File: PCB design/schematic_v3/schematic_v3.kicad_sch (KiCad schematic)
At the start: 111 parts, among them J1 Conn_01x05_Pin, J2 Conn_01x06_Pin, J3 Conn_01x03_Pin, J5 connection_moteur, Q1 IRLB8721PBF, SW1 SW_MEC_5E, U1 LAN9252, U2 STM32F446RETx, U3 HX1188NL, U4 XL1509-3.3, U5 24FC512-I/ST, U6 LMR14030SQDPRTQ1, U7 SP3485CN, Y1 25MHz, Y2 8MHz

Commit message: 03/06
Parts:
- removed C103, C104, C87, C88, C89, C90: 1u, symbol Device:C_Small
- removed C36: 47u, symbol Device:C_Polarized_Small_US
- removed C71: 10u, symbol Device:C_Small
- removed C72, C73: 2.2u, symbol Device:C_Small
- removed C85: 470u, symbol Device:C_Small
- removed C86: 330u, symbol Device:C_Small
- removed C91: 0.1, symbol Device:C_Small
- removed D2: B340, Diode_SMD:D_SMC, symbol Diode:B340
- removed F1: Bourns MF-MSMF250-2, symbol Device:Polyfuse_Small
- removed J1: Conn_01x05_Pin, symbol Connector:Conn_01x05_Pin
- removed J2: Conn_01x06_Pin, symbol Connector:Conn_01x06_Pin
- removed Q1: IRLB8721PBF, footprints:IRLB8721PBF, symbol IRLB8721PBF:IRLB8721PBF
- removed R45: 12.1k, symbol Device:R_Small
- removed SW1: SW_MEC_5E, Button_Switch_SMD:SW_MEC_5GSH9, symbol Switch:SW_MEC_5E
- removed U1: LAN9252, Package_DFN_QFN:QFN-64-1EP_9x9mm_P0.5mm_EP6x6mm, symbol LAN9252:LAN9252_test
- removed U4: XL1509-3.3, Package_SO:SOIC-8_3.9x4.9mm_P1.27mm, symbol Regulator_Switching:XL1509-3.3
- added C1, C11: 0.1u, Capacitor_SMD:C_0603_1608Metric, symbol Device:C_Small
- added C19, C20: 1u, Capacitor_SMD:C_0603_1608Metric, symbol Device:C_Small
- added C56: 10u, Capacitor_SMD:C_1206_3216Metric, symbol Device:C_Small
- added C57: 100n, Capacitor_SMD:C_0603_1608Metric, symbol Device:C_Small
- added C58, C59: 22u, Capacitor_SMD:C_1206_3216Metric, symbol Device:C_Small
- added IC1: LAN9252, footprints:LAN9252, symbol LAN9252:LAN9252
- added J1: Conn_01x04_Pin, Connector_JST:JST_EH_B4B-EH-A_1x04_P2.50mm_Vertical, symbol Connector:Conn_01x04_Pin
- added J3: Conn_01x05_Pin, Connector_PinHeader_1.27mm:PinHeader_1x05_P1.27mm_Vertical, symbol Connector:Conn_01x05_Pin
- added J5: Conn_01x02_Pin, Connector_JST:JST_EH_B2B-EH-A_1x02_P2.50mm_Vertical, symbol Connector:Conn_01x02_Pin
- added Q1: AO3400A, Package_TO_SOT_SMD:SOT-23, symbol Transistor_FET:AO3400A
- added R15, R17, R18: 10k, Resistor_SMD:R_0603_1608Metric, symbol Device:R_Small
- added R16: 12.1k, Resistor_SMD:R_0603_1608Metric, symbol Device:R_Small
- added S1: TS40-66-43-BK-260-SMT-TR, footprints:TS40-66-43-BK-260-SMT-TR, symbol TS40-66-43-BK-260-SMT-TR:TS40-66-43-BK-260-SMT-TR
- added U7: AP63203WU, Package_TO_SOT_SMD:TSOT-23-6, symbol Regulator_Switching:AP63203WU
- C10: renamed from C37; footprint (none) -> Capacitor_SMD:CP_Elec_5x5.4
- C12: renamed from C94; footprint (none) -> Capacitor_SMD:C_0603_1608Metric
- C13: renamed from C102; footprint (none) -> Capacitor_SMD:C_0603_1608Metric
- C14: renamed from C95; footprint (none) -> Capacitor_SMD:C_0603_1608Metric
- C15: renamed from C101; footprint (none) -> Capacitor_SMD:C_0603_1608Metric
- C16: renamed from C96; footprint (none) -> Capacitor_SMD:C_0603_1608Metric
- C17: renamed from C100; footprint (none) -> Capacitor_SMD:C_0603_1608Metric
- C18: renamed from C35; footprint (none) -> Capacitor_SMD:CP_Elec_5x5.4
- C2: renamed from C66; footprint (none) -> Capacitor_SMD:C_0603_1608Metric
- C21: renamed from C97; footprint (none) -> Capacitor_SMD:C_0603_1608Metric
- C22: renamed from C99; footprint (none) -> Capacitor_SMD:C_0603_1608Metric
- C26: renamed from C92; footprint (none) -> Capacitor_SMD:C_0603_1608Metric
- C27: renamed from C93; footprint (none) -> Capacitor_SMD:C_0603_1608Metric
- C28: renamed from C98; footprint (none) -> Capacitor_SMD:C_0603_1608Metric
- C29: renamed from C70; footprint (none) -> Capacitor_SMD:C_1206_3216Metric
- C3: renamed from C67; footprint (none) -> Capacitor_SMD:C_0603_1608Metric
- C30: renamed from C84; footprint (none) -> Capacitor_SMD:C_0603_1608Metric
- C33: renamed from C105; footprint (none) -> Capacitor_SMD:C_0603_1608Metric
- C35: renamed from C106; footprint (none) -> Capacitor_SMD:C_0603_1608Metric
- C38: renamed from C74; footprint (none) -> Capacitor_SMD:C_1206_3216Metric
- C39: renamed from C108; footprint (none) -> Capacitor_SMD:C_0603_1608Metric
- C4: renamed from C80; footprint (none) -> Capacitor_SMD:C_0603_1608Metric
- C40: renamed from C110; footprint (none) -> Capacitor_SMD:C_0603_1608Metric
- C41: renamed from C109; footprint (none) -> Capacitor_SMD:C_0603_1608Metric
- C42: renamed from C75; footprint (none) -> Capacitor_SMD:C_0603_1608Metric
- C43: renamed from C111; footprint (none) -> Capacitor_SMD:C_0603_1608Metric
- C44: renamed from C112; footprint (none) -> Capacitor_SMD:C_0603_1608Metric
- C45: renamed from C107; footprint (none) -> Capacitor_SMD:C_0603_1608Metric
- C46: renamed from C113; footprint (none) -> Capacitor_SMD:C_0603_1608Metric
- C47: renamed from C114; footprint (none) -> Capacitor_SMD:C_0603_1608Metric
- C48: renamed from C115; footprint (none) -> Capacitor_SMD:C_0603_1608Metric
- C5: renamed from C81; footprint (none) -> Capacitor_SMD:C_0603_1608Metric
- C50: renamed from C76; footprint (none) -> Capacitor_SMD:C_0603_1608Metric
- C51: renamed from C116; footprint (none) -> Capacitor_SMD:C_0603_1608Metric
- C52: renamed from C77; footprint (none) -> Capacitor_SMD:C_0603_1608Metric
- C53: renamed from C78; footprint (none) -> Capacitor_SMD:C_1206_3216Metric
- C55: renamed from C79; footprint (none) -> Capacitor_SMD:C_1206_3216Metric
- C6: renamed from C117; footprint (none) -> Capacitor_SMD:C_0603_1608Metric
- C7: renamed from C82; footprint (none) -> Capacitor_SMD:C_0603_1608Metric
- C8: renamed from C40; footprint (none) -> Capacitor_SMD:CP_Elec_5x5.4
- C9: renamed from C83; footprint (none) -> Capacitor_SMD:C_0603_1608Metric
- FB1, FB2, FB3, FB4: footprint footprints:LMR14030SQDPRTQ1 -> footprints:IND_BLM18_0603_MUR
- L1: footprint (none) -> Inductor_SMD:L_Bourns_SRR1260
- L3: value 47u -> 6.8u; footprint Inductor_SMD_Wurth:L_Wurth_WE-LQSH-4020 -> Inductor_SMD:L_Bourns-SRN4018; Field5 (none) -> 4040; Field6 (none) -> 3A
- R1: renamed from R30; footprint (none) -> Resistor_SMD:R_0603_1608Metric
- R10: renamed from R53; footprint (none) -> Resistor_SMD:R_0805_2012Metric
- R11: renamed from R35; footprint (none) -> Resistor_SMD:R_0603_1608Metric
- R12: renamed from R36; footprint (none) -> Resistor_SMD:R_0603_1608Metric
- R13: renamed from R58; footprint (none) -> Resistor_SMD:R_0603_1608Metric
- R14: renamed from R59; footprint (none) -> Resistor_SMD:R_0603_1608Metric
- R19: renamed from R42; footprint (none) -> Resistor_SMD:R_0603_1608Metric
- R2: renamed from R56; footprint (none) -> Resistor_SMD:R_0603_1608Metric
- R20: renamed from R46; footprint (none) -> Resistor_SMD:R_0603_1608Metric
- R21: renamed from R43; footprint (none) -> Resistor_SMD:R_0603_1608Metric
- R22: renamed from R44; footprint (none) -> Resistor_SMD:R_0603_1608Metric
- R23: renamed from R37; footprint (none) -> Resistor_SMD:R_0603_1608Metric
- R24: renamed from R38; footprint (none) -> Resistor_SMD:R_0603_1608Metric
- R25: renamed from R39; footprint (none) -> Resistor_SMD:R_0603_1608Metric
- R26: renamed from R47; footprint (none) -> Resistor_SMD:R_0603_1608Metric
- R27: renamed from R52; footprint (none) -> Resistor_SMD:R_0603_1608Metric
- R28: renamed from R40; footprint (none) -> Resistor_SMD:R_0603_1608Metric
- R29: renamed from R41; footprint (none) -> Resistor_SMD:R_0603_1608Metric
- R3: renamed from R57; footprint (none) -> Resistor_SMD:R_0603_1608Metric
- R30: renamed from R48; footprint (none) -> Resistor_SMD:R_0603_1608Metric
- R31: renamed from R51; footprint (none) -> Resistor_SMD:R_0603_1608Metric
- R32: renamed from R49; footprint (none) -> Resistor_SMD:R_0603_1608Metric
- R33: renamed from R50; footprint (none) -> Resistor_SMD:R_0603_1608Metric
- R4: renamed from R31; footprint (none) -> Resistor_SMD:R_0603_1608Metric
- R5: renamed from R32; footprint (none) -> Resistor_SMD:R_0603_1608Metric
- R6: renamed from R33; footprint (none) -> Resistor_SMD:R_0603_1608Metric
- R7: renamed from R34; footprint (none) -> Resistor_SMD:R_0603_1608Metric
- R8: renamed from R54; footprint (none) -> Resistor_SMD:R_0603_1608Metric
- R9: renamed from R55; footprint (none) -> Resistor_SMD:R_0603_1608Metric
- renumbered D4 to D1, D5 to D2, FB6 to FB5, J5 to J2, J3 to J4, U3 to U1, U7 to U2, U5 to U3, U6 to U4, U2 to U5
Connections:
- net VDD12TX is gone; now on net +3.3V: FB4.2
- net VDD12TX2 is gone; now on net VDD12TX1: C33.1
- net +12V: now also D1.2 (A), C56.1, U7.2 (EN), U7.3 (IN); no longer D1.1 (K)
- net +3.3V: now also FB1.1, C58.1, C59.1, IC1.14 (VDDIO0), IC1.20 (VDDIO1), IC1.32 (VDDIO2), IC1.37 (VDDIO3), IC1.47 (VDDIO4), IC1.5 (VDD33), IC1.7 (REG_EN), J3.4 (Pin_4), R15.1, U7.1 (FB); no longer FB1.2, FB2.2
- net GND: now also C1.1, C11.1, C19.2, C20.2, C56.2, C58.2, C59.2, IC1.10 (FXSDB/FXLOSB/FXSDENB), IC1.4 (OSCVSS), IC1.40 (D8/AD8/DIGIO2/GPI2/GPO2/MII_MDIO), IC1.41 (TESTMODE), IC1.65 (VSS), IC1.8 (FXLOSEN), IC1.9 (FXSDA/FXLOSA/FXSDENA), J3.3 (Pin_3), J5.1 (Pin_1), Q1.2 (S), R16.1, R17.1, R18.1, S1.1 (COM_1), S1.2 (COM_2), U7.4 (GND)
- net I2C_SCL: now also IC1.43 (EESCL/TCK)
- net I2C_SDL: now also IC1.42 (EESDA/TMS)
- net IRQ: now also IC1.44 (IRQ)
- net MISO: now also IC1.13 (D1/AD1/EOF/SO/SIO1)
- net MOSI: now also IC1.17 (D0/AD0/WD_STATE/SI/SIO0)
- net NRST: now also J3.5 (Pin_5), S1.3 (NO_1), S1.4 (NO_2)
- net OSCI: now also IC1.1 (OSCI)
- net OSCO: now also IC1.2 (OSCO)
- net RST#: now also IC1.11 (RST#)
- net RXA_N: now also IC1.54 (RXNA)
- net RXA_P: now also IC1.55 (RXPA)
- net SCK: now also IC1.19 (D9/AD9/LATCH_IN/SCK)
- net SCS#: now also IC1.50 (D5/AD5/OUTVALID/SCS#)
- net SWCLK: now also J3.2 (Pin_2)
- net SWDIO: now also J3.1 (Pin_1)
- net SYNC0: now also IC1.34 (SYNC0/LATCH0)
- net TXA_N: now also IC1.52 (TXNA)
- net TXA_P: now also IC1.53 (TXPA)
- net VDD12TX1: now also FB2.2, IC1.56 (VDD12TX1), IC1.59 (VDD12TX2)
- net VDD33TXRX1: now also FB3.1, C19.1, IC1.51 (VDD33TXRX1); no longer FB1.1
- net VDD33TXRX2: now also FB4.1, C20.1, IC1.64 (VDD33TXRX2); no longer FB2.1
- net VDDCR: now also FB2.1, C1.2, IC1.24 (VDDCR1), IC1.3 (OSCVDD12), IC1.38 (VDDCR2), IC1.6 (VDDCR0); no longer FB4.1
- net +36V: now reaches D2.2 (A)
- net +36V: now also J5.2 (Pin_2)
- net at U1.11 (RX+): now also J1.2 (Pin_2)
- net at U1.14 (TX-): now also J1.3 (Pin_3)
- net at U1.16 (TX+): now also J1.4 (Pin_4)
- net at U1.9 (RX-): now also J1.1 (Pin_1)
- net at L3.1: now also C57.1, U7.5 (SW)
- net at J2.1 (Pin_1): now also D1.1 (K), Q1.3 (D); no longer D1.2 (A)
- net at R13.1, R14.2: now also Q1.1 (G)
- net at U5.14 (PA0): now also J4.2 (Pin_2); no longer J4.3 (Pin_3)
- net at U5.15 (PA1): now also J4.3 (Pin_3); no longer J4.2 (Pin_2)
- net SMPS_PGOOD: no longer names the net of R23.2, R24.1, U4.8 (PGOOD)
- new net: IC1.48 (LINKACTLED0/TDO/CHIP_MODE0), R18.2
- new net: IC1.57 (RBIAS), R16.2
- new net: IC1.46 (LINKACTLED1/TDI/CHIP_MODE1), R17.2
- new net: C11.2, FB1.2, IC1.58 (VDD33BIAS)
- new net: C57.2, U7.6 (BST)
- new net: IC1.45 (RUNLED/E2PSIZE), R15.2
- no-connect marks 59 -> 55
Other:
- note added: "(Reused from previous project)"
- note added: "(Safety: Cut motor power)"
- note added: "+12V to +3.3V Converter"
- note added: "Add COPPER POUR (GND)"
- note added: "Limit Switch Input (Initialization)"
- note added: "Motor Power Output"
- note added: "Pogo pin connector interface"
- note removed: "(Récupéré sur le projet précédent)"
- note removed: "(Sécurité : couper l'alimentation moteur)"
- note removed: "Ajouter PLAN DE MASSE !"
- note removed: "Composant pour passer via les connecteurs pogo"
- note removed: "Entrée Capteur fin de course (Initialisation)"
- note removed: "Sortie Alimentation Moteur"
- note removed: "convertisseur +12V -> +3.3V"
- company: (none) -> Heemskerk Innovative Technology (HIT)
- title: (none) -> EtherCAT -> Dynamixel XM430 W350
- moved on the sheet: C10, C12, C13, C14, C15, C16, C17, C18, C2, C21, C22, C26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

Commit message: pcb updated
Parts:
- removed S1: TS40-66-43-BK-260-SMT-TR, footprints:TS40-66-43-BK-260-SMT-TR, symbol TS40-66-43-BK-260-SMT-TR:TS40-66-43-BK-260-SMT-TR
- added F1: 2920L150_60MR, footprints:2920L150_60MR, symbol 2920L150_60MR:2920L150_60MR
- added H1, H2, H3, H4: MountingHole, MountingHole:MountingHole_3.2mm_M3_Pad_Via, symbol Mechanical:MountingHole
- added S1: B3U-1100PM, footprints:B3U1100PM, symbol B3U-1100PM:B3U-1100PM
- C1, C11, C13, C15, C16, C17: value 0.1u -> 100n
- C20: renamed from C21; value 0.1u -> 100n
- C21: renamed from C22; value 0.1u -> 100n
- C24: renamed from C28; value 0.1u -> 100n
- C25: renamed from C30; value 0.1u -> 100n
- C27: renamed from C33; value 0.1u -> 100n
- C28: renamed from C35; value 0.1u -> 100n
- C5: renamed from C6; value 0.1u -> 100n
- J5: renamed from J4; footprint Connector_PinHeader_1.27mm:PinHeader_1x03_P1.27mm_Vertical -> Connector_JST:JST_EH_B3B-EH-A_1x03_P2.50mm_Vertical
- R16: value 12.1k -> 12k
- renumbered C9 to C10, C19 to C18, C20 to C19, C26 to C22, C27 to C23, C18 to C26, C38 to C30, C39 to C31, C40 to C32, C41 to C33, C42 to C34, C43 to C35, C44 to C36, C45 to C37, C46 to C38, C56 to C39, C47 to C40, C48 to C41, C50 to C42, C51 to C43, C52 to C44, C57 to C45, C53 to C46, C58 to C47, C55 to C48, C59 to C49, C5 to C6, C10 to C9, J5 to J2, J2 to J3, J3 to J4, L3 to L2, R2 to R1, R1 to R2, U2 to U1, U1 to U2, U7 to U6
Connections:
- net +12V: now also D1.1 (K); no longer D1.2 (A)
- net +36V: now also F1.1; no longer D2.2 (A)
- net GND: now also S1.2 (NO), S1.3 (GND)
- net NRST: now also S1.1 (COM)
- net VIN: now reaches C26.1, C29.1, C30.1, D2.1 (K), R23.1, U4.2 (VIN), U4.3 (VIN), U4.4 (EN)
- net VDD48: now reaches C41.2, U5.48 (VDD)
- net PA5: now reaches R30.2, U5.21 (PA5)
- net PH1: now reaches C33.2, U5.6 (PH1), Y2.1
- net PH0: now reaches C32.2, U5.5 (PH0), Y2.2
- net CMT2: now reaches R12.2, U2.10 (CMT)
- net RX_P: now reaches J1.2 (Pin_2), U2.11 (RX+)
- net TX_N: now reaches J1.3 (Pin_3), U2.14 (TX-)
- net CMT1: now reaches R11.2, U2.15 (CMT)
- net TX_P: now reaches J1.4 (Pin_4), U2.16 (TX+)
- net TCT: now reaches C7.1, R7.2, U2.2 (TCT), U2.7 (RCT)
- net RX_N: now reaches J1.1 (Pin_1), U2.9 (RX-)
- net DATA+: now reaches J3.3 (Pin_3), R10.2, R8.1, U1.6 (A)
- net RBIAS: now reaches IC1.57 (RBIAS), R16.2
- net DRAIN: now reaches J3.1 (Pin_1), Q1.3 (D)
- net DRAIN: now also D1.2 (A); no longer D1.1 (K)
- net DE/RE: now reaches R3.1, U1.2 (~{RE}), U1.3 (DE)
- net DATA-: now reaches J3.4 (Pin_4), R10.1, R9.2, U1.7 (B)
- net PA7: now reaches R33.2, U5.23 (PA7)
- net BOOT0: now reaches R26.1, U5.60 (BOOT0)
- net VDD32: now reaches C40.2, U5.32 (VDD)
- net VDD64: now reaches C43.2, U5.64 (VDD)
- net SW: now reaches C45.1, L2.1, U6.5 (SW)
- net SS: now reaches C34.1, U4.6 (SS)
- net BOOT: now reaches C42.1, U4.1 (BOOT)
- net VDD19: now reaches C38.2, U5.19 (VDD)
- net AX: now reaches R19.1, U3.1 (A0), U3.2 (A1), U3.3 (A2), U3.7 (WP)
- net VDD33BIAS: now reaches C11.2, FB1.2, IC1.58 (VDD33BIAS)
- net CMT: now reaches C10.1, R11.1, R12.1
- net FB: now reaches C44.2, R28.2, R29.1, U4.7 (FB)
- net VCAP_1: now reaches C37.1, U5.30 (VCAP_1)
- net BST: now reaches C45.2, U6.6 (BST)
- net GATE: now reaches Q1.1 (G), R13.1, R14.2
- net PGOOD: now reaches R23.2, R24.1, U4.8 (PGOOD)
- net PA6: now reaches R32.2, U5.22 (PA6)
- net PA0: now reaches J5.2 (Pin_2), U5.14 (PA0)
- net PA1: now reaches U5.15 (PA1)
- net PA1: now also J5.1 (Pin_1); no longer J5.3 (Pin_3)
- net PA4: now reaches U5.20 (PA4)
- net PA4: now also J5.3 (Pin_3); no longer J5.1 (Pin_1)
- net RT_SYNC: now reaches R25.1, U4.5 (RT_SYNC)
- new net: D2.2 (A), F1.2
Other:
- note added: "Mounting Hole"
- note added: "Reset Button"
- note removed: "Add COPPER POUR (GND)"
- note removed: "Bouton Reset"
- moved on the sheet: C37, D1, J5, R16, R30, R32, R33

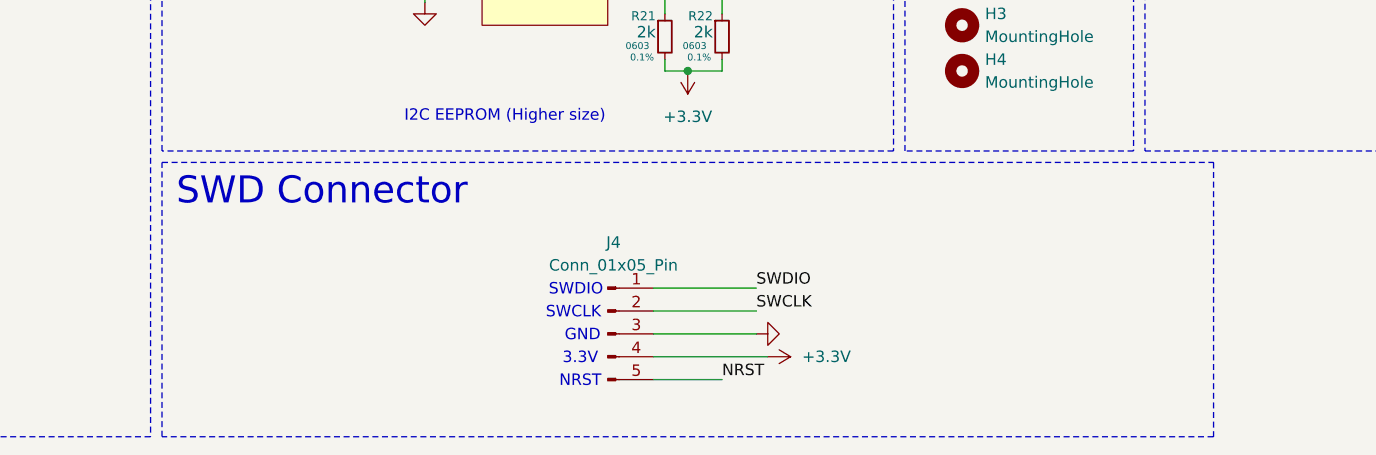
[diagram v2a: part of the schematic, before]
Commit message: 1KHz ecat communication frequency done
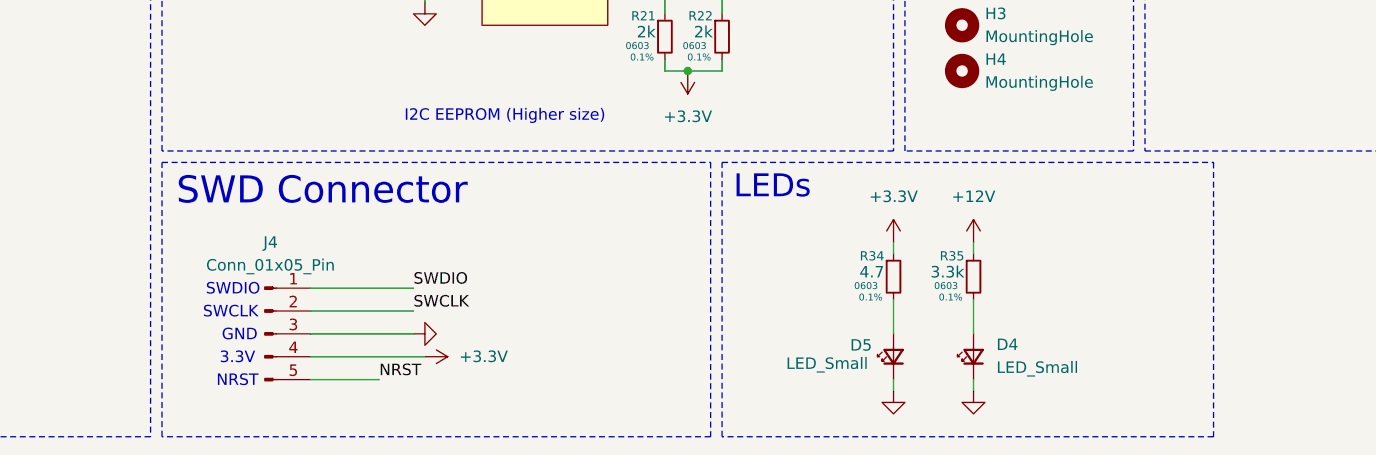
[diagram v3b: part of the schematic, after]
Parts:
- added D4, D5: LED_Small, LED_SMD:LED_0201_0603Metric, symbol Device:LED_Small
- added R34: 4.7, Resistor_SMD:R_0603_1608Metric, symbol Device:R_Small
- added R35: 3.3k, Resistor_SMD:R_0603_1608Metric, symbol Device:R_Small
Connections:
- net +12V: now also R35.1
- net +3.3V: now also R34.1
- net GND: now also D4.1 (K), D5.1 (K)
- new net: D4.2 (A), R35.2
- new net: D5.2 (A), R34.2
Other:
- note added: "LEDs"
- moved on the sheet: J4
